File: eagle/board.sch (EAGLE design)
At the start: 9 parts, among them J1 M20X2SHROUDED

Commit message: Add cap to switches for debounce
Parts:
- added C1, C2: 10nF, SparkFun-Passives:CAPPTH
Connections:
- new net N$19: C1.2, S1.1
- new net N$20: C1.1, S1.2
- new net N$21: C2.1, S2.1
- new net N$22: C2.2, S2.2
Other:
- moved on the sheet: S2
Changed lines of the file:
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@@
 <part name="RFID" library="SparkFun-Connectors" deviceset="M06" device="LOCK"/>
 <part name="GSM" library="SparkFun-Connectors" deviceset="M06" device="LOCK"/>
+<part name="C1" library="SparkFun-Passives" deviceset="CAP" device="PTH" value="10nF"/>
+<part name="C2" library="SparkFun-Passives" deviceset="CAP" device="PTH" value="10nF"/>
 </parts>
 <sheets>
@@
 <instance part="J1" gate="G$1" x="68.58" y="91.44"/>
 <instance part="S1" gate="G$1" x="119.38" y="63.5"/>
-<instance part="S2" gate="G$1" x="119.38" y="50.8"/>
+<instance part="S2" gate="G$1" x="185.42" y="60.96"/>
 <instance part="FRAME1" gate="G$1" x="0" y="0"/>
 <instance part="FRAME1" gate="V" x="147.32" y="0"/>
@@
 <instance part="RFID" gate="G$1" x="12.7" y="99.06"/>
 <instance part="GSM" gate="G$1" x="12.7" y="68.58"/>
+<instance part="C1" gate="G$1" x="119.38" y="55.88" rot="R270"/>
+<instance part="C2" gate="G$1" x="187.96" y="53.34" rot="R90"/>
 </instances>
 <busses>
@@
 </segment>
 </net>
+<net name="N$19" class="0">
+<segment>
+<pinref part="S1" gate="G$1" pin="1"/>
+<pinref part="C1" gate="G$1" pin="2"/>
+<wire x1="114.3" y1="63.5" x2="114.3" y2="58.42" width="0.1524" layer="91"/>
+<wire x1="114.3" y1="58.42" x2="116.84" y2="55.88" width="0.1524" layer="91"/>
+</segment>
+</net>
+<net name="N$20" class="0">
+<segment>
+<pinref part="S1" gate="G$1" pin="2"/>
+<pinref part="C1" gate="G$1" pin="1"/>
+<wire x1="124.46" y1="63.5" x2="124.46" y2="55.88" width="0.1524" layer="91"/>
+</segment>
+</net>
+<net name="N$21" class="0">
+<segment>
+<pinref part="S2" gate="G$1" pin="1"/>
+<pinref part="C2" gate="G$1" pin="1"/>
+<wire x1="180.34" y1="60.96" x2="180.34" y2="55.88" width="0.1524" layer="91"/>
+<wire x1="180.34" y1="55.88" x2="182.88" y2="53.34" width="0.1524" layer="91"/>
+</segment>
+</net>
+<net name="N$22" class="0">
+<segment>
+<pinref part="S2" gate="G$1" pin="2"/>
+<pinref part="C2" gate="G$1" pin="2"/>
+<wire x1="190.5" y1="60.96" x2="190.5" y2="53.34" width="0.1524" layer="91"/>
+</segment>
+</net>

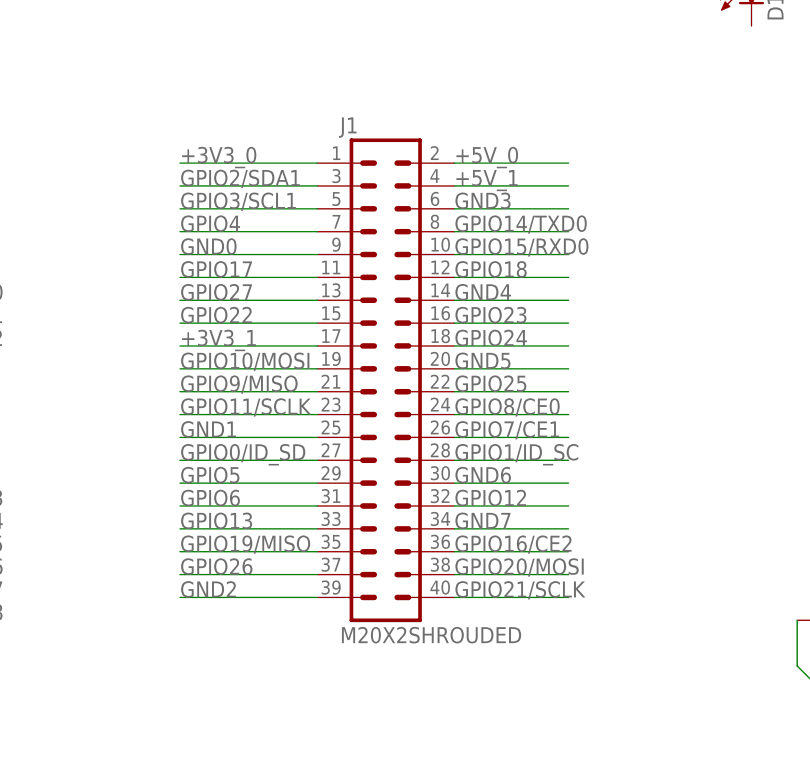
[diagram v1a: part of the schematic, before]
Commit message: Rename nets on ribbon connector
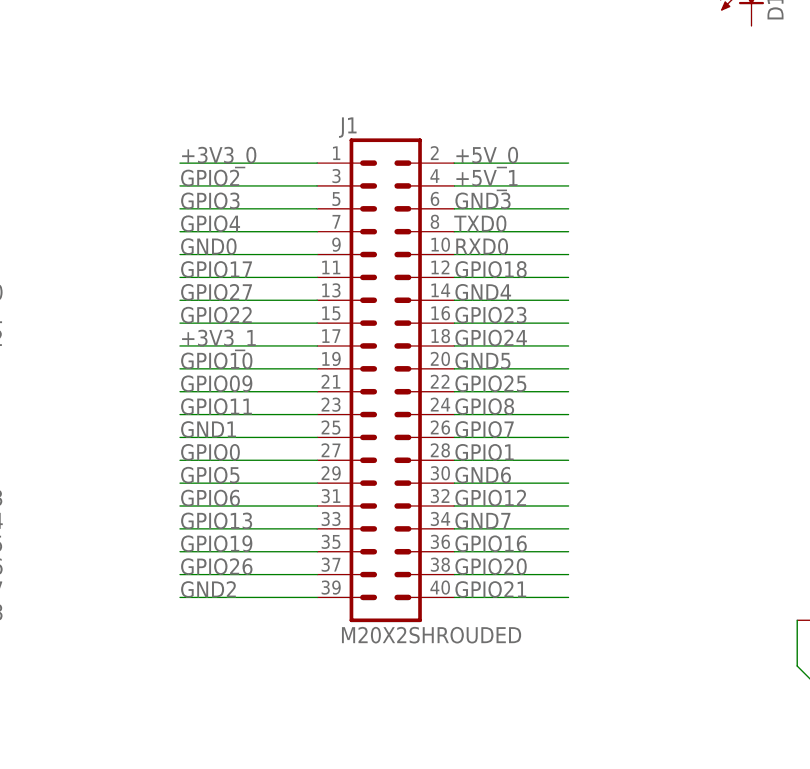
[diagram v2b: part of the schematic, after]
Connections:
- net GPIO1/ID_SC renamed GPIO1
- net GPIO10/MOSI renamed GPIO10
- net GPIO11/SCLK renamed GPIO11
- net GPIO14/TXD0 renamed TXD0
- net GPIO15/RXD0 renamed RXD0
- net GPIO16/CE2 renamed GPIO16
- net GPIO19/MISO renamed GPIO19
- net GPIO2/SDA1 renamed GPIO2
- net GPIO20/MOSI renamed GPIO20
- net GPIO21/SCLK renamed GPIO21
- net GPIO3/SCL1 renamed GPIO3
- net GPIO7/CE1 renamed GPIO7
- net GPIO8/CE0 renamed GPIO8
- net GPIO9/MISO renamed GPIO09
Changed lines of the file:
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@@
 </segment>
 </net>
-<net name="GPIO14/TXD0" class="0">
+<net name="TXD0" class="0">
 <segment>
 <pinref part="J1" gate="G$1" pin="8"/>
@@
 </segment>
 </net>
-<net name="GPIO15/RXD0" class="0">
+<net name="RXD0" class="0">
 <segment>
 <pinref part="J1" gate="G$1" pin="10"/>
@@
 </segment>
 </net>
-<net name="GPIO8/CE0" class="0">
+<net name="GPIO8" class="0">
 <segment>
 <pinref part="J1" gate="G$1" pin="24"/>
@@
 </segment>
 </net>
-<net name="GPIO7/CE1" class="0">
+<net name="GPIO7" class="0">
 <segment>
 <pinref part="J1" gate="G$1" pin="26"/>
@@
 </segment>
 </net>
-<net name="GPIO1/ID_SC" class="0">
+<net name="GPIO1" class="0">
 <segment>
 <pinref part="J1" gate="G$1" pin="28"/>
@@
 </segment>
 </net>
-<net name="GPIO16/CE2" class="0">
+<net name="GPIO16" class="0">
 <segment>
 <pinref part="J1" gate="G$1" pin="36"/>
@@
 </segment>
 </net>
-<net name="GPIO20/MOSI" class="0">
+<net name="GPIO20" class="0">
 <segment>
 <pinref part="J1" gate="G$1" pin="38"/>
@@
 </segment>
 </net>
-<net name="GPIO21/SCLK" class="0">
+<net name="GPIO21" class="0">
 <segment>
 <pinref part="J1" gate="G$1" pin="40"/>
@@
 </segment>
 </net>
-<net name="GPIO2/SDA1" class="0">
+<net name="GPIO2" class="0">
 <segment>
 <pinref part="J1" gate="G$1" pin="3"/>
@@
 </segment>
 </net>
-<net name="GPIO3/SCL1" class="0">
+<net name="GPIO3" class="0">
 <segment>
 <pinref part="J1" gate="G$1" pin="5"/>
@@
 </segment>
 </net>
-<net name="GPIO9/MISO" class="0">
+<net name="GPIO09" class="0">
 <segment>
 <pinref part="J1" gate="G$1" pin="21"/>
@@
 </segment>
 </net>
-<net name="GPIO11/SCLK" class="0">
+<net name="GPIO11" class="0">
 <segment>
 <pinref part="J1" gate="G$1" pin="23"/>
@@
 </segment>
 </net>
-<net name="GPIO19/MISO" class="0">
+<net name="GPIO19" class="0">
 <segment>
 <pinref part="J1" gate="G$1" pin="35"/>
@@
 </segment>
 </net>
-<net name="GPIO0/ID_SD" class="0">
+<net name="GPIO0" class="0">
 <segment>
 <wire x1="60.96" y1="81.28" x2="45.72" y2="81.28" width="0.1524" layer="91"/>
@@
 </segment>
 </net>
-<net name="GPIO10/MOSI" class="0">
+<net name="GPIO10" class="0">
 <segment>
 <pinref part="J1" gate="G$1" pin="19"/>

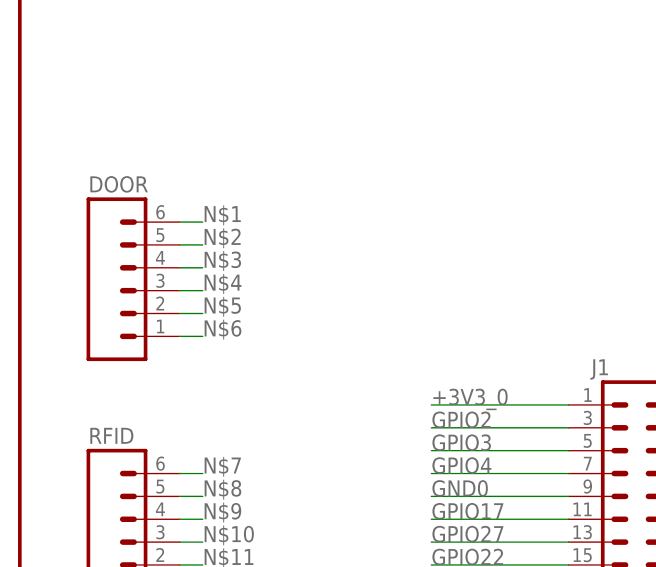
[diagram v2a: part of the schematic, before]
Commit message: Connect door header
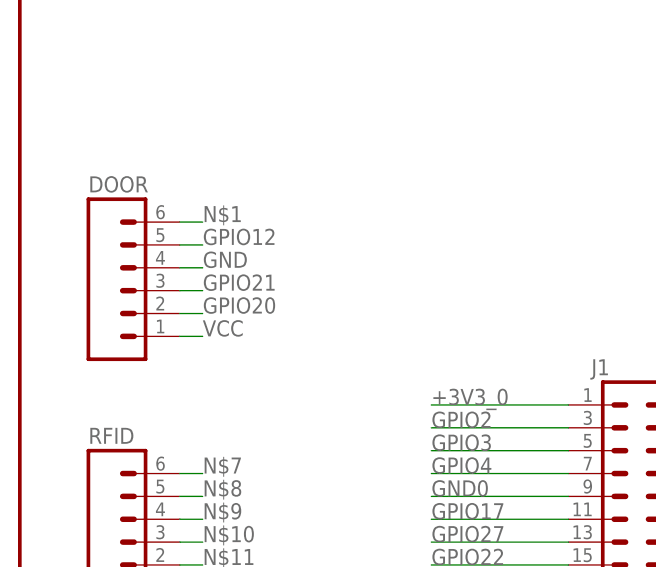
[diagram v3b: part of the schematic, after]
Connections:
- net N$3 renamed GND
- net N$6 renamed VCC
- removed net N$2: DOOR.5
- removed net N$4: DOOR.3
- removed net N$5: DOOR.2
- net GPIO12: now also DOOR.5
- net GPIO20: now also DOOR.2
- net GPIO21: now also DOOR.3
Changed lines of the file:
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@@
 <label x="76.2" y="76.2" size="1.778" layer="95"/>
+</segment>
+<segment>
+<pinref part="DOOR" gate="G$1" pin="5"/>
+<wire x1="17.78" y1="132.08" x2="20.32" y2="132.08" width="0.1524" layer="91"/>
+<label x="20.32" y="132.08" size="1.778" layer="95"/>
 </segment>
 </net>
@@
 <label x="76.2" y="68.58" size="1.778" layer="95"/>
 </segment>
+<segment>
+<pinref part="DOOR" gate="G$1" pin="2"/>
+<wire x1="17.78" y1="124.46" x2="20.32" y2="124.46" width="0.1524" layer="91"/>
+<label x="20.32" y="124.46" size="1.778" layer="95"/>
+</segment>
 </net>
 <net name="GPIO21" class="0">
@@
 <label x="76.2" y="66.04" size="1.778" layer="95"/>
 </segment>
+<segment>
+<pinref part="DOOR" gate="G$1" pin="3"/>
+<wire x1="17.78" y1="127" x2="20.32" y2="127" width="0.1524" layer="91"/>
+<label x="20.32" y="127" size="1.778" layer="95"/>
+</segment>
 </net>
 <net name="+3V3_1" class="0">
@@
 </segment>
 </net>
-<net name="N$2" class="0">
-<segment>
-<pinref part="DOOR" gate="G$1" pin="5"/>
-<wire x1="17.78" y1="132.08" x2="20.32" y2="132.08" width="0.1524" layer="91"/>
-<label x="20.32" y="132.08" size="1.778" layer="95"/>
-</segment>
-</net>
-<net name="N$3" class="0">
+<net name="GND" class="0">
 <segment>
 <pinref part="DOOR" gate="G$1" pin="4"/>
@@
 </segment>
 </net>
-<net name="N$4" class="0">
-<segment>
-<pinref part="DOOR" gate="G$1" pin="3"/>
-<wire x1="17.78" y1="127" x2="20.32" y2="127" width="0.1524" layer="91"/>
-<label x="20.32" y="127" size="1.778" layer="95"/>
-</segment>
-</net>
-<net name="N$5" class="0">
-<segment>
-<pinref part="DOOR" gate="G$1" pin="2"/>
-<wire x1="17.78" y1="124.46" x2="20.32" y2="124.46" width="0.1524" layer="91"/>
-<label x="20.32" y="124.46" size="1.778" layer="95"/>
-</segment>
-</net>
-<net name="N$6" class="0">
+<net name="VCC" class="0">
 <segment>
 <pinref part="DOOR" gate="G$1" pin="1"/>

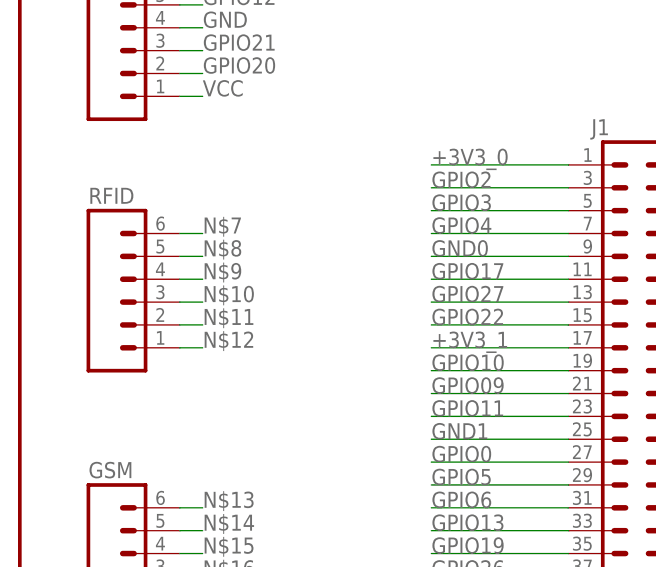
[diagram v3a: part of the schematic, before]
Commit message: Connect rfid header
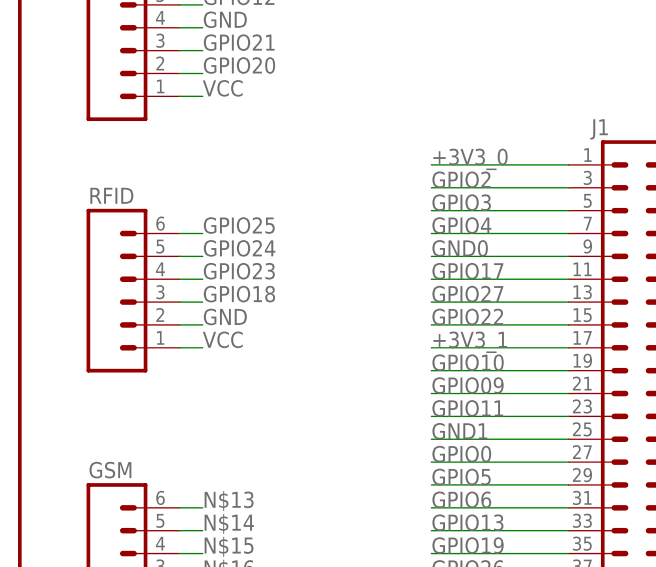
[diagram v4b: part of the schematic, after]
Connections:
- removed net N$10: RFID.3
- removed net N$11: RFID.2
- removed net N$12: RFID.1
- removed net N$7: RFID.6
- removed net N$8: RFID.5
- removed net N$9: RFID.4
- net GND: now also RFID.2
- net GPIO18: now also RFID.3
- net GPIO23: now also RFID.4
- net GPIO24: now also RFID.5
- net GPIO25: now also RFID.6
- net VCC: now also RFID.1
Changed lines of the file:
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@@
 <label x="76.2" y="101.6" size="1.778" layer="95"/>
+</segment>
+<segment>
+<pinref part="RFID" gate="G$1" pin="3"/>
+<wire x1="17.78" y1="99.06" x2="20.32" y2="99.06" width="0.1524" layer="91"/>
+<label x="20.32" y="99.06" size="1.778" layer="95"/>
 </segment>
 </net>
@@
 <label x="76.2" y="96.52" size="1.778" layer="95"/>
 </segment>
+<segment>
+<pinref part="RFID" gate="G$1" pin="4"/>
+<wire x1="17.78" y1="101.6" x2="20.32" y2="101.6" width="0.1524" layer="91"/>
+<label x="20.32" y="101.6" size="1.778" layer="95"/>
+</segment>
 </net>
 <net name="GPIO24" class="0">
@@
 <label x="76.2" y="93.98" size="1.778" layer="95"/>
 </segment>
+<segment>
+<pinref part="RFID" gate="G$1" pin="5"/>
+<wire x1="17.78" y1="104.14" x2="20.32" y2="104.14" width="0.1524" layer="91"/>
+<label x="20.32" y="104.14" size="1.778" layer="95"/>
+</segment>
 </net>
 <net name="GPIO25" class="0">
@@
 <label x="76.2" y="88.9" size="1.778" layer="95"/>
 </segment>
+<segment>
+<pinref part="RFID" gate="G$1" pin="6"/>
+<wire x1="17.78" y1="106.68" x2="20.32" y2="106.68" width="0.1524" layer="91"/>
+<label x="20.32" y="106.68" size="1.778" layer="95"/>
+</segment>
 </net>
 <net name="GPIO8" class="0">
@@
 <label x="20.32" y="129.54" size="1.778" layer="95"/>
 </segment>
+<segment>
+<pinref part="RFID" gate="G$1" pin="2"/>
+<wire x1="17.78" y1="96.52" x2="20.32" y2="96.52" width="0.1524" layer="91"/>
+<label x="20.32" y="96.52" size="1.778" layer="95"/>
+</segment>
 </net>
 <net name="VCC" class="0">
@@
 <label x="20.32" y="121.92" size="1.778" layer="95"/>
 </segment>
-</net>
-<net name="N$7" class="0">
-<segment>
-<pinref part="RFID" gate="G$1" pin="6"/>
-<wire x1="17.78" y1="106.68" x2="20.32" y2="106.68" width="0.1524" layer="91"/>
-<label x="20.32" y="106.68" size="1.778" layer="95"/>
-</segment>
-</net>
-<net name="N$8" class="0">
-<segment>
-<pinref part="RFID" gate="G$1" pin="5"/>
-<wire x1="17.78" y1="104.14" x2="20.32" y2="104.14" width="0.1524" layer="91"/>
-<label x="20.32" y="104.14" size="1.778" layer="95"/>
-</segment>
-</net>
-<net name="N$9" class="0">
-<segment>
-<pinref part="RFID" gate="G$1" pin="4"/>
-<wire x1="17.78" y1="101.6" x2="20.32" y2="101.6" width="0.1524" layer="91"/>
-<label x="20.32" y="101.6" size="1.778" layer="95"/>
-</segment>
-</net>
-<net name="N$10" class="0">
-<segment>
-<pinref part="RFID" gate="G$1" pin="3"/>
-<wire x1="17.78" y1="99.06" x2="20.32" y2="99.06" width="0.1524" layer="91"/>
-<label x="20.32" y="99.06" size="1.778" layer="95"/>
-</segment>
-</net>
-<net name="N$11" class="0">
-<segment>
-<pinref part="RFID" gate="G$1" pin="2"/>
-<wire x1="17.78" y1="96.52" x2="20.32" y2="96.52" width="0.1524" layer="91"/>
-<label x="20.32" y="96.52" size="1.778" layer="95"/>
-</segment>
-</net>
-<net name="N$12" class="0">
 <segment>
 <pinref part="RFID" gate="G$1" pin="1"/>

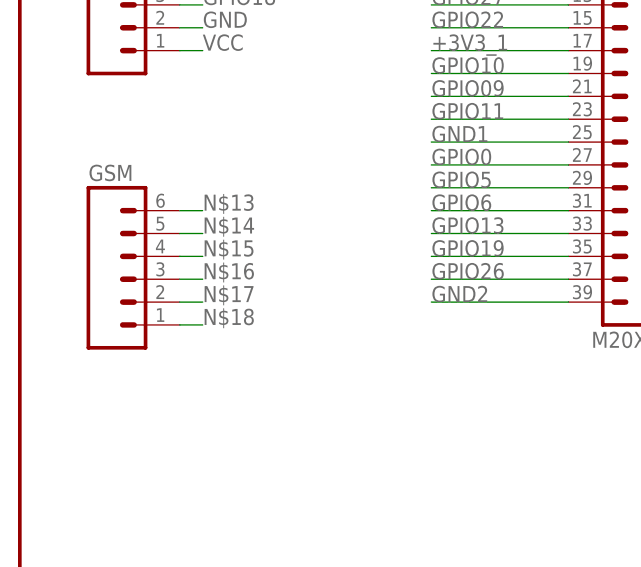
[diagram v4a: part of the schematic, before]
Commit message: Connect gsm header
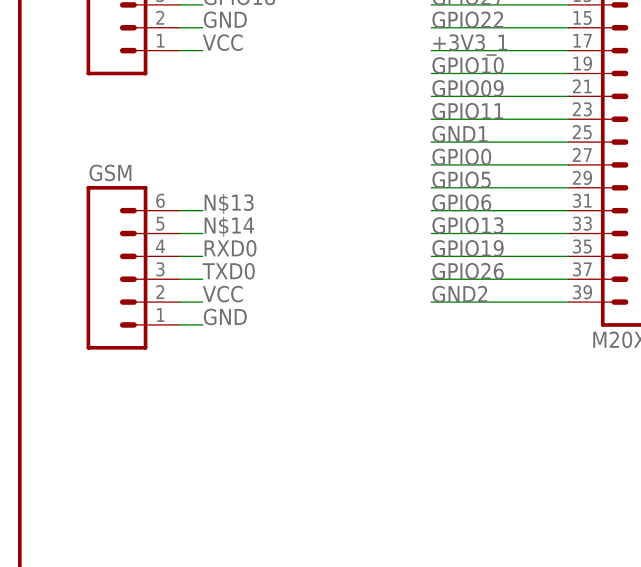
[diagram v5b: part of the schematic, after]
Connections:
- removed net N$15: GSM.4
- removed net N$16: GSM.3
- removed net N$17: GSM.2
- removed net N$18: GSM.1
- net GND: now also GSM.1
- net RXD0: now also GSM.4
- net TXD0: now also GSM.3
- net VCC: now also GSM.2
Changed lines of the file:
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@@
 <label x="76.2" y="106.68" size="1.778" layer="95"/>
+</segment>
+<segment>
+<pinref part="GSM" gate="G$1" pin="3"/>
+<wire x1="20.32" y1="68.58" x2="17.78" y2="68.58" width="0.1524" layer="91"/>
+<label x="20.32" y="68.58" size="1.778" layer="95"/>
 </segment>
 </net>
@@
 <label x="76.2" y="104.14" size="1.778" layer="95"/>
 </segment>
+<segment>
+<pinref part="GSM" gate="G$1" pin="4"/>
+<wire x1="17.78" y1="71.12" x2="20.32" y2="71.12" width="0.1524" layer="91"/>
+<label x="20.32" y="71.12" size="1.778" layer="95"/>
+</segment>
 </net>
 <net name="GPIO18" class="0">
@@
 <label x="20.32" y="96.52" size="1.778" layer="95"/>
 </segment>
+<segment>
+<pinref part="GSM" gate="G$1" pin="1"/>
+<wire x1="17.78" y1="63.5" x2="20.32" y2="63.5" width="0.1524" layer="91"/>
+<label x="20.32" y="63.5" size="1.778" layer="95"/>
+</segment>
 </net>
 <net name="VCC" class="0">
@@
 <label x="20.32" y="93.98" size="1.778" layer="95"/>
 </segment>
+<segment>
+<pinref part="GSM" gate="G$1" pin="2"/>
+<wire x1="17.78" y1="66.04" x2="20.32" y2="66.04" width="0.1524" layer="91"/>
+<label x="20.32" y="66.04" size="1.778" layer="95"/>
+</segment>
 </net>
 <net name="N$13" class="0">
@@
 </segment>
 </net>
-<net name="N$15" class="0">
-<segment>
-<pinref part="GSM" gate="G$1" pin="4"/>
-<wire x1="17.78" y1="71.12" x2="20.32" y2="71.12" width="0.1524" layer="91"/>
-<label x="20.32" y="71.12" size="1.778" layer="95"/>
-</segment>
-</net>
-<net name="N$16" class="0">
-<segment>
-<pinref part="GSM" gate="G$1" pin="3"/>
-<wire x1="20.32" y1="68.58" x2="17.78" y2="68.58" width="0.1524" layer="91"/>
-<label x="20.32" y="68.58" size="1.778" layer="95"/>
-</segment>
-</net>
-<net name="N$17" class="0">
-<segment>
-<pinref part="GSM" gate="G$1" pin="2"/>
-<wire x1="17.78" y1="66.04" x2="20.32" y2="66.04" width="0.1524" layer="91"/>
-<label x="20.32" y="66.04" size="1.778" layer="95"/>
-</segment>
-</net>
-<net name="N$18" class="0">
-<segment>
-<pinref part="GSM" gate="G$1" pin="1"/>
-<wire x1="17.78" y1="63.5" x2="20.32" y2="63.5" width="0.1524" layer="91"/>
-<label x="20.32" y="63.5" size="1.778" layer="95"/>
-</segment>
-</net>
